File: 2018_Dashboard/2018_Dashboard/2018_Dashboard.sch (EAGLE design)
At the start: 51 parts, among them Y1 16MHz

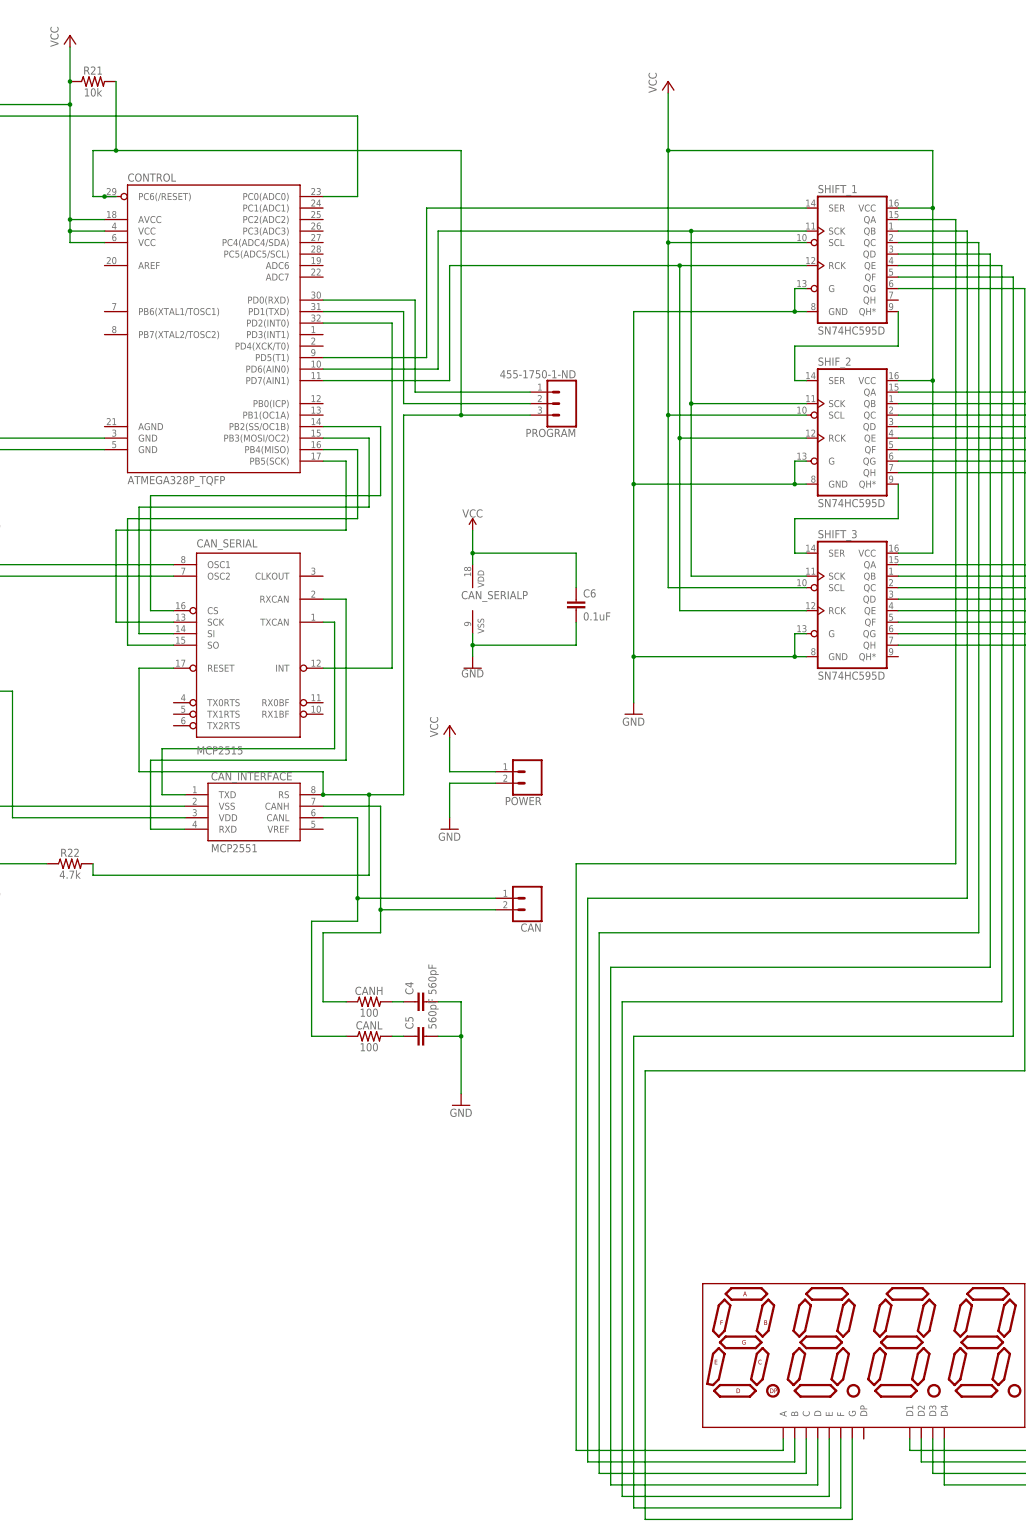
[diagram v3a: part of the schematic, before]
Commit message: Fix "board and schematic are not consistent"
Also wired up the decimal point because why not
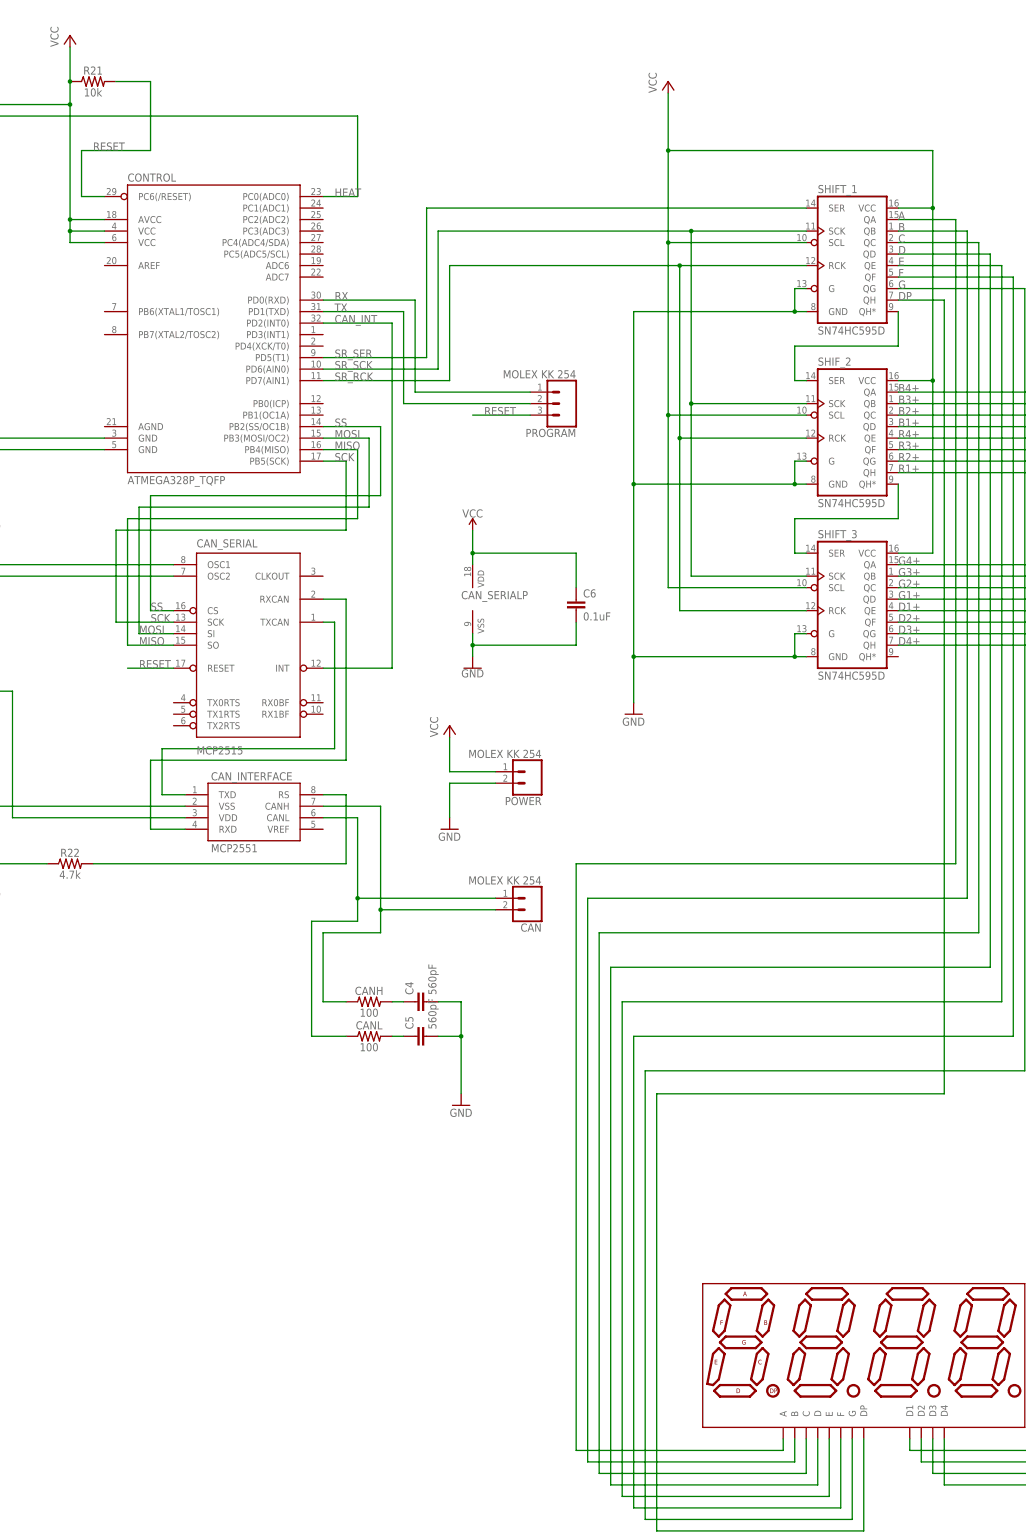
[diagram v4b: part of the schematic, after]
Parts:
- CAN, POWER: value (none) -> MOLEX KK 254
- PROGRAM: value 455-1750-1-ND -> MOLEX KK 254
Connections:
- net N$10 renamed CARRY2
- net N$11 renamed A
- net N$12 renamed B
- net N$13 renamed C
- net N$14 renamed D
- net N$15 renamed E
- net N$16 renamed F
- net N$17 renamed G
- net N$18 renamed B2
- net N$19 renamed B3
- net N$2 renamed CARRY1
- net N$20 renamed SR_SER
- net N$21 renamed SR_SCK
- net N$22 renamed SR_RCK
- net N$23 renamed B4
- net N$24 renamed D1
- net N$25 renamed B4+
- net N$26 renamed B3+
- net N$27 renamed B2+
- net N$28 renamed B1+
- net N$29 renamed G1
- net N$3 renamed D1+
- net N$30 renamed G2
- net N$31 renamed G3
- net N$32 renamed G4
- net N$33 renamed R1
- net N$34 renamed R2
- net N$35 renamed R3
- net N$36 renamed R4
- net N$37 renamed B1
- net N$39 renamed R4+
- net N$4 renamed D2+
- net N$40 renamed R3+
- net N$41 renamed R2+
- net N$42 renamed R1+
- net N$43 renamed G4+
- net N$44 renamed G3+
- net N$45 renamed G2+
- net N$46 renamed G1+
- net N$47 renamed D2
- net N$48 renamed D3
- net N$49 renamed D4
- net N$5 renamed D3+
- net N$50 renamed HEAT+
- net N$51 renamed HEAT
- net N$52 renamed SS
- net N$53 renamed MOSI
- net N$54 renamed MISO
- net N$55 renamed SCK
- net N$56 renamed CAN_INT
- net N$59 renamed OSC2
- net N$6 renamed D4+
- net N$62 renamed CHI
- net N$63 renamed OSC1
- net N$65 renamed CLI
- net N$67 renamed RX
- net N$68 renamed TX
- removed net N$61: CAN_INTERFACE.RS, CAN_SERIAL>NAME.RESET, CONTROL.PC6(/RESET), PROGRAM.3, R21.2, R22.2
- new net CI_SLOPE: CAN_INTERFACE.RS, R22.2
- new net DP: SEVEN_SEGMENT.DP, SHIFT_1.QH
- new net RESET: CAN_SERIAL>NAME.RESET, CONTROL.PC6(/RESET), PROGRAM.3, R21.2
